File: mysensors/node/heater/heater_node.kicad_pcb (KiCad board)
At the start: 2 copper layers, 40 parts, among them CON1 AVR-ISP-10, IC1 ATMEGA328P-A, P1 UART_CONSOLE, P2 ANTENNA, Q1 BC337, SW1 RESET, U1 RFM69HW, U2 HLK-PM01, U3 AMS1117-3.3, X1 230Vac~~, X2 16MHz, X3 HEATER_SW

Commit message: mysensors heater node pcb routing 1st pass
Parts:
- added REF**: 1pin, Connect:1pin, F.Cu at (174.1, 51.1)
- added REF**: 1pin, Connect:1pin, F.Cu at (102.0, 124.7)
- added REF**: 1pin, Connect:1pin, F.Cu at (173.9, 106.9)
- added REF**: 1pin, Connect:1pin, F.Cu at (101.6, 51.3)
- moved D1 58.5 mm to (151.4, 121.7)
- moved R7 58.5 mm to (151.4, 114.0)
- moved X2 38.7 mm to (127.9, 94.4)
- moved C4 37.9 mm to (133.1, 113.4)
- moved C6 37.9 mm to (137.1, 113.6)
- moved C8 37.9 mm to (128.2, 84.9)
- moved C9 37.9 mm to (106.2, 89.9)
- moved F1 37.9 mm to (161.0, 69.2)
- moved IC1 37.9 mm to (136.9, 104.6)
- moved R1 37.9 mm to (135.8, 120.2), turned to 270 degrees
- moved R5 37.9 mm to (122.6, 105.4)
- moved U1 37.9 mm to (118.6, 96.6)
- moved U3 37.9 mm to (119.4, 84.4)
- moved C3 37.7 mm to (134.8, 94.1)
- moved R11 37.3 mm to (127.5, 119.6)
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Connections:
- C7 pad 2: Net-(C7-Pad2) -> /RST
- IC1 pad 29: Net-(C7-Pad2) -> /RST
- R1 pad 2: Net-(C7-Pad2) -> /RST
- SW1 pad 1: Net-(C7-Pad2) -> /RST
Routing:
- net GND: track 0.00 -> 163.4 mm
- net +5V: track 0.00 -> 85.4 mm
- net /MISO: track 0.00 -> 62.2 mm, vias 0 -> 2
- net /RST: track 0.00 -> 45.5 mm, vias 0 -> 2
- net /MOSI: track 0.00 -> 41.9 mm, vias 0 -> 1
- net Net-(U2-Pad2): track 0.00 -> 38.5 mm
- net /HEATER_ON_LED: track 0.00 -> 33.2 mm
- net /INT: track 0.00 -> 31.6 mm, vias 0 -> 2
- net Net-(F1-Pad2): track 0.00 -> 30.0 mm
- net Net-(RL1-Pad11): track 0.00 -> 26.8 mm
- net /ERR_LED: track 0.00 -> 26.1 mm
- net Net-(R2-Pad1): track 0.00 -> 24.8 mm
- net Net-(R10-Pad1): track 0.00 -> 22.6 mm
- net /TX_LED: track 0.00 -> 20.4 mm
- net Net-(R4-Pad1): track 0.00 -> 17.6 mm
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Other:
- board outline added: 79.4 x 80.6 mm
- board text added: "High voltage!"
- board text added: "L N"

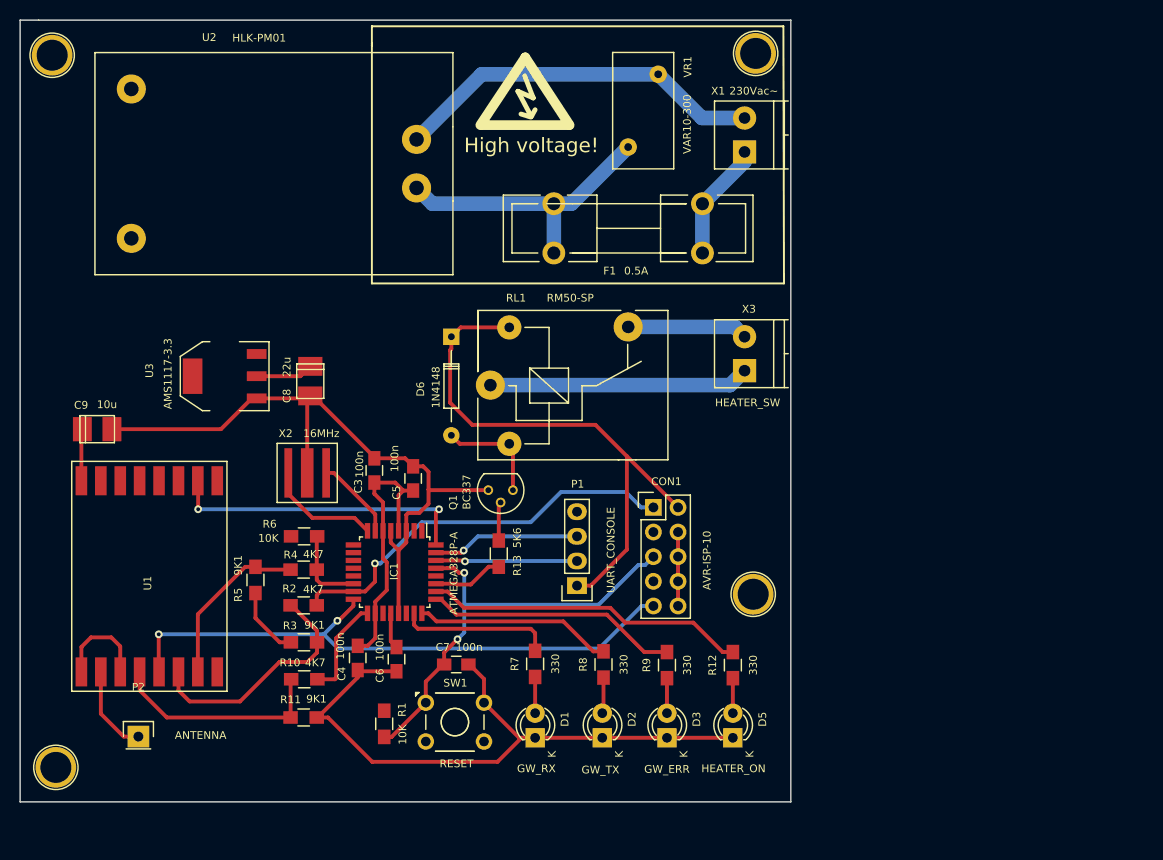
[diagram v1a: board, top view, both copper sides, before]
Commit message: mysensors heater node pcb routing 2nd pass
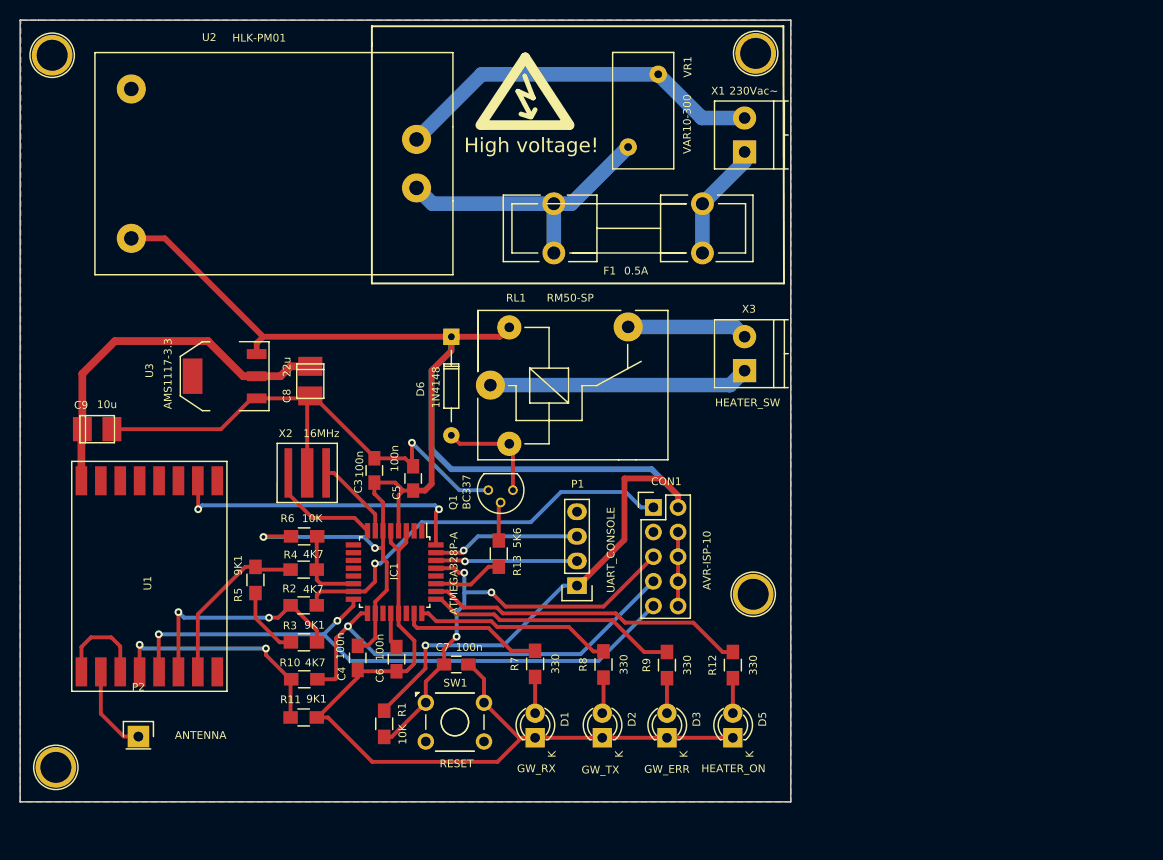
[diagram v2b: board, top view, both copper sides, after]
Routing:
- net +5V: track 85.4 -> 195.7 mm, vias 0 -> 3
- net /SCK: track 10.4 -> 46.2 mm, vias 0 -> 1
- net +3V3: track 11.3 -> 37.9 mm
- net GND: track 163.4 -> 168.1 mm, vias 0 -> 1
- net Net-(R10-Pad1): track 22.6 -> 24.2 mm, vias 0 -> 2
- net Net-(R2-Pad1): track 24.8 -> 23.5 mm, vias 0 -> 2
- net /RX_LED: track 15.8 -> 14.8 mm
- net /MISO: track 62.2 -> 63.3 mm
- net /RST: track 45.5 -> 46.2 mm, vias 2 -> 3
- added copper zone on B.Cu, net GND
- added copper zone on F.Cu, net GND

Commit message: mysensors heater added node id config switch
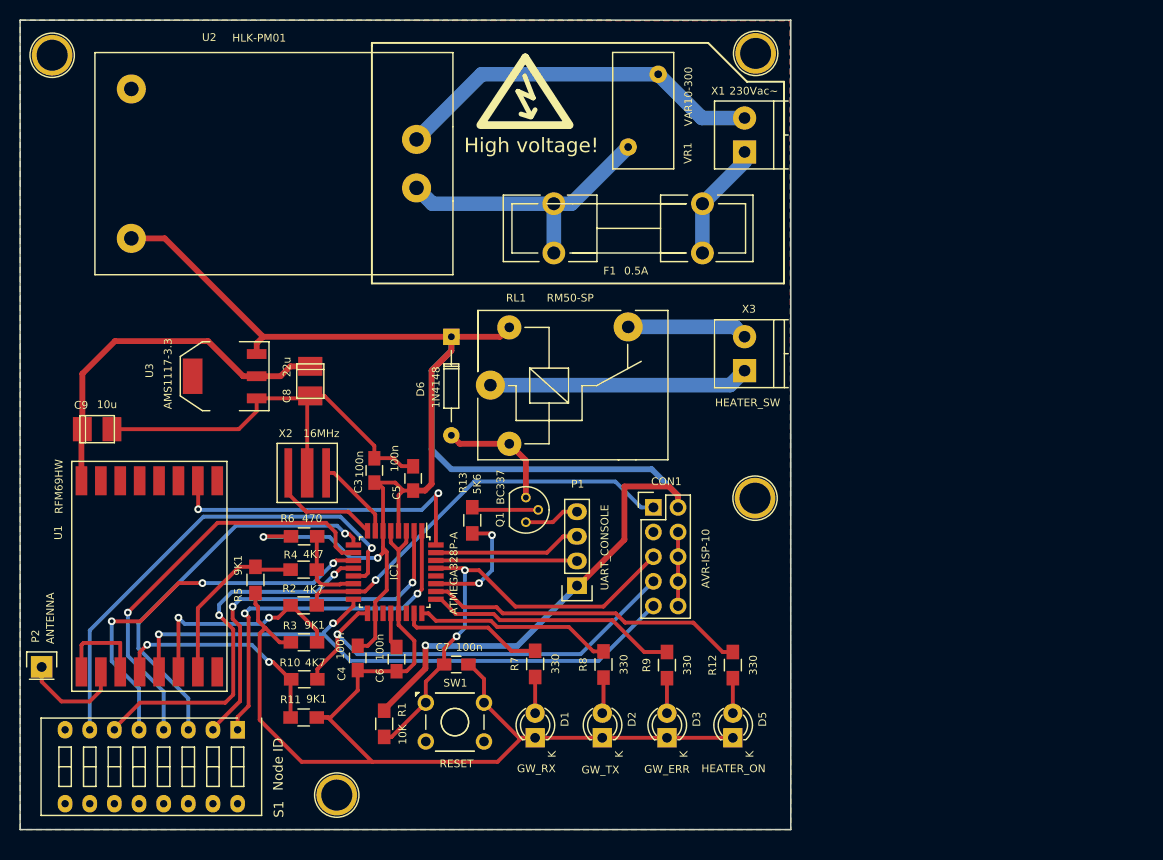
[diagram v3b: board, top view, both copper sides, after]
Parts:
- added S1: Node ID, Buttons_Switches_ThroughHole:SW_DIP_x8_Slide, F.Cu at (120.7, 120.8)
- R6: value 10K -> 470
- moved REF** 29.1 mm to (130.9, 127.6)
- moved P2 12.3 mm to (100.5, 114.4)
- moved REF** 9.91 mm to (174.1, 97.0)
- moved R13 4.38 mm to (144.9, 99.3)
- moved Q1 1.54 mm to (150.4, 96.9), turned to 270 degrees
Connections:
- IC1 pad 1: Net-(IC1-Pad1) -> /C0
- IC1 pad 10: Net-(IC1-Pad10) -> /C3
- IC1 pad 11: Net-(IC1-Pad11) -> /C4
- IC1 pad 12: Net-(IC1-Pad12) -> /C5
- IC1 pad 13: Net-(IC1-Pad13) -> /C6
- IC1 pad 2: Net-(IC1-Pad2) -> /C1
- IC1 pad 9: Net-(IC1-Pad9) -> /C2
- REF** pad : GND -> (no net)
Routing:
- net /C6: track 0.00 -> 49.9 mm, vias 0 -> 1
- net /C3: track 0.00 -> 42.8 mm, vias 0 -> 1
- net /C2: track 0.00 -> 40.7 mm, vias 0 -> 1
- net /C4: track 0.00 -> 39.9 mm, vias 0 -> 3
- net /C5: track 0.00 -> 39.3 mm, vias 0 -> 2
- net /C1: track 0.00 -> 39.1 mm, vias 0 -> 2
- net /C0: track 0.00 -> 37.9 mm, vias 0 -> 2
- net GND: track 168.1 -> 186.8 mm, vias 1 -> 0
- net /H_RELAY_CMD: track 7.28 -> 12.1 mm, vias 0 -> 2
- net Net-(Q1-Pad2): track 4.00 -> 6.91 mm
- net /INT: track 31.9 -> 33.9 mm
- net Net-(P2-Pad1): track 9.16 -> 10.8 mm
- net Net-(D6-Pad2): track 11.3 -> 12.6 mm
- net /RST: track 46.2 -> 47.3 mm, vias 3 -> 2
- net Net-(R10-Pad1): track 24.2 -> 23.4 mm
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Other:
- board size 79.4 x 80.6 mm -> 79.4 x 83.4 mm

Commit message: mysensors heater node pcb routing 3rd pass
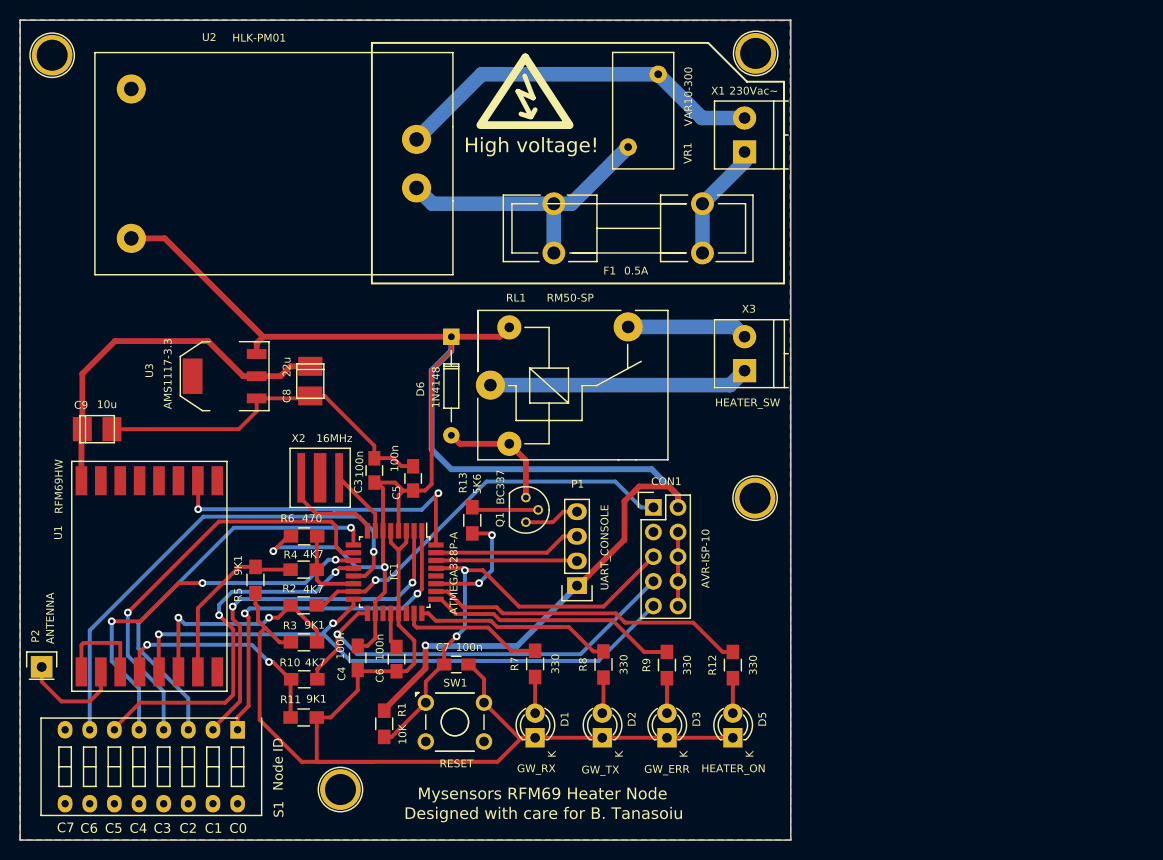
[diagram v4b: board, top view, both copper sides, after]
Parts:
- added REF**: my_logo, myfootprints:my_logo, B.Cu at (173.1, 108.9)
- moved X2 1.43 mm to (129.2, 94.9)
- moved REF** 0.69 mm to (131.3, 127.0)
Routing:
- net GND: track 186.8 -> 181.9 mm
- net +5V: track 196.0 -> 193.1 mm
- net Net-(IC1-Pad7): track 8.54 -> 7.02 mm
- net /C6: track 49.9 -> 51.2 mm
- net Net-(IC1-Pad8): track 11.8 -> 10.7 mm
- net /MOSI: track 41.8 -> 41.1 mm
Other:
- board size 79.4 x 83.4 mm -> 79.4 x 84.5 mm
- board text added: "C0"
- board text added: "C1"
- board text added: "C2"
- board text added: "C3"
- board text added: "C4"
- board text added: "C5"
- board text added: "C6"
- board text added: "C7"
- board text added: "Designed with care for B. Tanasoiu"
- board text added: "Mysensors RFM69 Heater Node"

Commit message: mysensors heater node pcb final touches
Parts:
- added REF**: 1pin, Connect:1pin, F.Cu at (101.7, 80.1)
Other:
- board text added: "Antenna Length: 433 MHz -> 165 mm 868 MHz -> 82 mm 915 MHz -> 78 mm"
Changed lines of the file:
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@@
 (kicad_pcb (version 4) (host pcbnew 4.1.0-alpha+201606210817+6944~45~ubuntu14.04.1-product)
   (general
-    (links 108)
+    (links 109)
     (no_connects 0)
     (area 97.745499 46.312 179.6417 132.282001)
     (thickness 1.6)
-    (drawings 53)
+    (drawings 54)
     (tracks 387)
     (zones 0)
-    (modules 46)
+    (modules 47)
     (nets 54)
   )
@@
     (visible_elements FFFFFF7F)
     (pcbplotparams
-      (layerselection 0x00030_80000001)
-      (usegerberextensions false)
-      (excludeedgelayer true)
+      (layerselection 0x030f0_ffffffff)
+      (usegerberextensions true)
+      (excludeedgelayer false)
       (linewidth 0.100000)
       (plotframeref false)
@@
       (plotinvisibletext false)
       (padsonsilk false)
-      (subtractmaskfromsilk false)
+      (subtractmaskfromsilk true)
       (outputformat 1)
       (mirror false)
-      (drillshape 1)
+      (drillshape 0)
       (scaleselection 1)
-      (outputdirectory ""))
+      (outputdirectory gerber/))
   )
   (net 0 "")
@@
   )
   (module Connect:1pin (layer F.Cu)
+    (at 101.727 80.0735)
+    (descr "module 1 pin (ou trou mecanique de percage)")
+    (tags DEV)
+    (fp_text reference REF** (at 0 -3.048) (layer F.SilkS) hide
+      (effects (font (size 1 1) (thickness 0.15)))
+    )
+    (fp_text value 1pin (at 0 2.794) (layer F.Fab) hide
+      (effects (font (size 1 1) (thickness 0.15)))
+    )
+    (fp_circle (center 0 0) (end 0 -2.286) (layer F.SilkS) (width 0.15))
+    (pad "" thru_hole circle (at 0 0) (size 4.2 4.2) (drill 3.2) (layers *.Cu *.Mask)
+      (net 2 GND) (zone_connect 2))
+  )
+  (module Connect:1pin (layer F.Cu)
     (at 174.117 51.1175)
     (descr "module 1 pin (ou trou mecanique de percage)")
@@
     (tags "capacitor 0805")
     (attr smd)
-    (fp_text reference C3 (at -1.631 -1.651 90) (layer F.SilkS)
-      (effects (font (size 0.8 0.8) (thickness 0.15)))
-    )
-    (fp_text value 100n (at 1.2265 2.0955 90) (layer F.SilkS)
+    (fp_text reference C3 (at -2.159 -1.651 90) (layer F.SilkS)
+      (effects (font (size 0.8 0.8) (thickness 0.15)))
+    )
+    (fp_text value 100n (at 0.508 2.286 90) (layer F.SilkS)
       (effects (font (size 0.8 0.8) (thickness 0.15)))
     )
@@
     (tags "capacitor 0805")
     (attr smd)
-    (fp_text reference C5 (at 1.4605 1.7145 270) (layer F.SilkS)
-      (effects (font (size 0.8 0.8) (thickness 0.15)))
-    )
-    (fp_text value 100n (at -1.4605 5.5245 270) (layer F.SilkS)
+    (fp_text reference C5 (at 1.5875 1.7145 270) (layer F.SilkS)
+      (effects (font (size 0.8 0.8) (thickness 0.15)))
+    )
+    (fp_text value 100n (at -1.524 5.715 270) (layer F.SilkS)
       (effects (font (size 0.8 0.8) (thickness 0.15)))
     )
@@
     (tags "QFP 0.8")
     (attr smd)
-    (fp_text reference IC1 (at -0.0635 0.0635 270) (layer F.SilkS)
-      (effects (font (size 0.8 0.8) (thickness 0.15)))
-    )
-    (fp_text value ATMEGA328P-A (at 0.127 -6.096 270) (layer F.SilkS)
+    (fp_text reference IC1 (at 4.826 -6.1595 270) (layer F.SilkS)
+      (effects (font (size 0.8 0.8) (thickness 0.15)))
+    )
+    (fp_text value ATMEGA328P-A (at -1.397 -6.223 270) (layer F.SilkS)
       (effects (font (size 0.8 0.8) (thickness 0.15)))
     )
@@
     (tags "resistor 0805")
     (attr smd)
-    (fp_text reference R7 (at 0 -2.1 90) (layer F.SilkS)
-      (effects (font (size 0.8 0.8) (thickness 0.15)))
-    )
-    (fp_text value 330 (at 0 2.1 90) (layer F.SilkS)
+    (fp_text reference R7 (at -1.5875 -1.778 90) (layer F.SilkS)
+      (effects (font (size 0.8 0.8) (thickness 0.15)))
+    )
+    (fp_text value 330 (at 1.016 -1.7145 90) (layer F.SilkS)
       (effects (font (size 0.8 0.8) (thickness 0.15)))
     )
@@
     (tags "resistor 0805")
     (attr smd)
-    (fp_text reference R8 (at 0 -2.1 90) (layer F.SilkS)
-      (effects (font (size 0.8 0.8) (thickness 0.15)))
-    )
-    (fp_text value 330 (at 0 2.1 90) (layer F.SilkS)
+    (fp_text reference R8 (at -1.524 -1.778 90) (layer F.SilkS)
+      (effects (font (size 0.8 0.8) (thickness 0.15)))
+    )
+    (fp_text value 330 (at 1.016 -1.778 90) (layer F.SilkS)
       (effects (font (size 0.8 0.8) (thickness 0.15)))
     )
@@
     (tags "resistor 0805")
     (attr smd)
-    (fp_text reference R9 (at 0 -2.1 90) (layer F.SilkS)
-      (effects (font (size 0.8 0.8) (thickness 0.15)))
-    )
-    (fp_text value 330 (at 0 2.1 90) (layer F.SilkS)
+    (fp_text reference R9 (at -1.5875 -1.905 90) (layer F.SilkS)
+      (effects (font (size 0.8 0.8) (thickness 0.15)))
+    )
+    (fp_text value 330 (at 1.143 -1.778 90) (layer F.SilkS)
       (effects (font (size 0.8 0.8) (thickness 0.15)))
     )
@@
     (tags "resistor 0805")
     (attr smd)
-    (fp_text reference R12 (at 0 -2.1 90) (layer F.SilkS)
-      (effects (font (size 0.8 0.8) (thickness 0.15)))
-    )
-    (fp_text value 330 (at 0 2.1 90) (layer F.SilkS)
+    (fp_text reference R12 (at -1.4605 -1.905 90) (layer F.SilkS)
+      (effects (font (size 0.8 0.8) (thickness 0.15)))
+    )
+    (fp_text value 330 (at 1.4605 -1.8415 90) (layer F.SilkS)
       (effects (font (size 0.8 0.8) (thickness 0.15)))
     )
@@
     (fp_line (start 2.1082 -0.0762) (end 2.1082 -2.3448) (layer B.SilkS) (width 0.5))
     (fp_line (start 3.2592 -0.0762) (end 0.9906 -0.0762) (layer B.SilkS) (width 0.5))
+  )
+  (gr_text "Antenna Length:\n433 MHz -> 165 mm\n868 MHz ->  82 mm\n915 MHz ->  78 mm" (at 103.505 98.425 90) (layer B.SilkS)
+    (effects (font (size 1.2 1.2) (thickness 0.2)) (justify mirror))
   )
   (gr_text C7 (at 102.997 130.937) (layer F.SilkS)
@@
     (polygon
       (pts
-        (xy 126.9365 48.0695) (xy 126.9365 77.724) (xy 140.081 77.724) (xy 140.081 92.456) (xy 177.7365 92.456)
+        (xy 126.9365 48.0695) (xy 126.9365 81.153) (xy 140.081 81.153) (xy 140.081 92.456) (xy 177.7365 92.456)
         (xy 177.673 47.6885) (xy 126.9365 47.752)
       )
@@
     (polygon
       (pts
-        (xy 126.873 47.988799) (xy 126.873 77.643299) (xy 140.0175 77.643299) (xy 140.0175 92.375299) (xy 177.673 92.375299)
+        (xy 126.873 47.988799) (xy 126.9365 81.153) (xy 140.081 81.153) (xy 140.081 92.456) (xy 177.7365 92.456)
         (xy 177.673 47.752) (xy 126.873 47.671299)
       )
